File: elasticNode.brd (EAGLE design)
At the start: 58.2 x 52.5 mm, 117 parts, among them J1 FEMALE_HEADER_2X1, J2 JUMPER, J3 ISP_CONN_6PIN, J4 FEMALE_HEADER_3X2, J5 FEMALE_HEADER_10X2, J6 USB_CONNMICRO_SMT, M1 SISS23DN, M2 SISS23DN, M3 SISS23DN, U1 AT90USB128, U10 LTC3419DFN, U11 PAC1720, U12 MT41J128M8, U14 LTC3419DFN, U2 ATMEGA64AQFN, U3 MRF24J40MA, U4 SPARTAN7-LX15, U6 SST26VF032BWDFN, U7 PAC1720, U8 PAC1720, U9 PAC1720, X1 8MHz, X2 50MHz, X3 32MHz, X4 100MHz

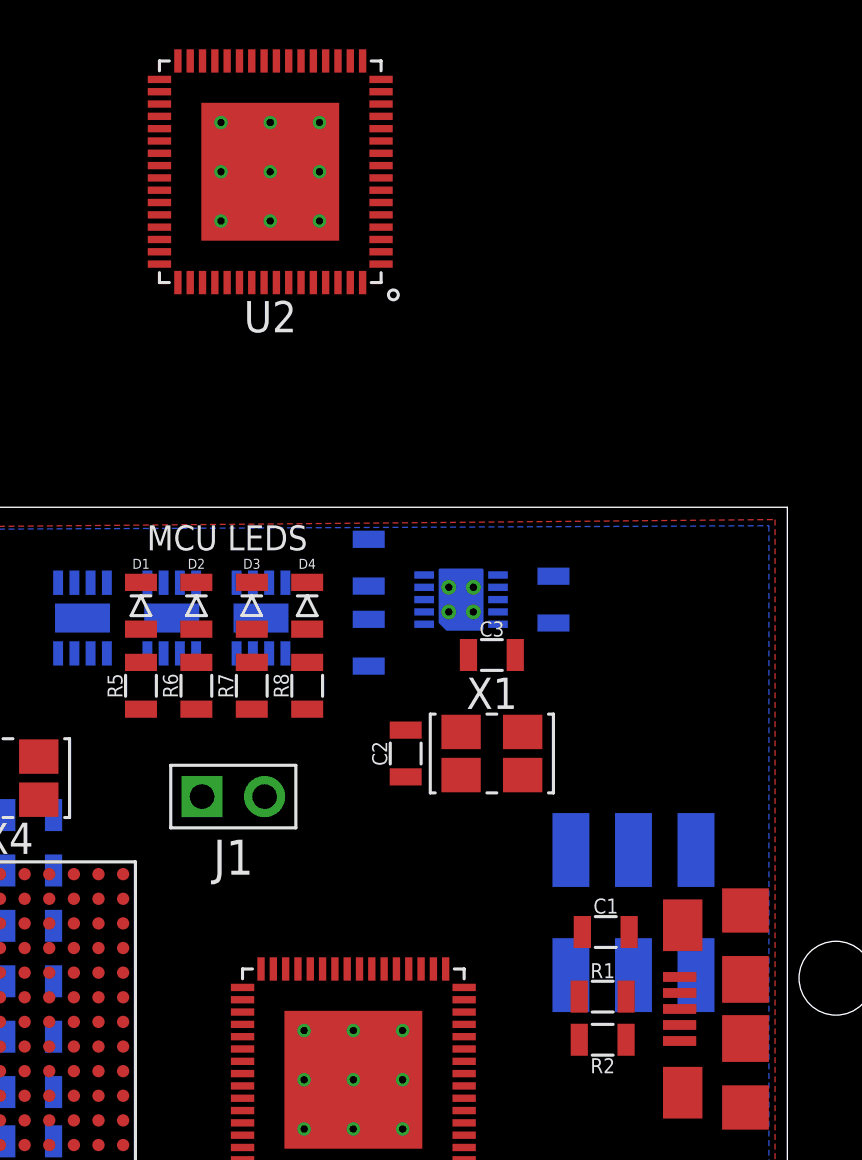
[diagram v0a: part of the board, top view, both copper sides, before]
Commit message: Remove old MCU
 working on the mother board interface.
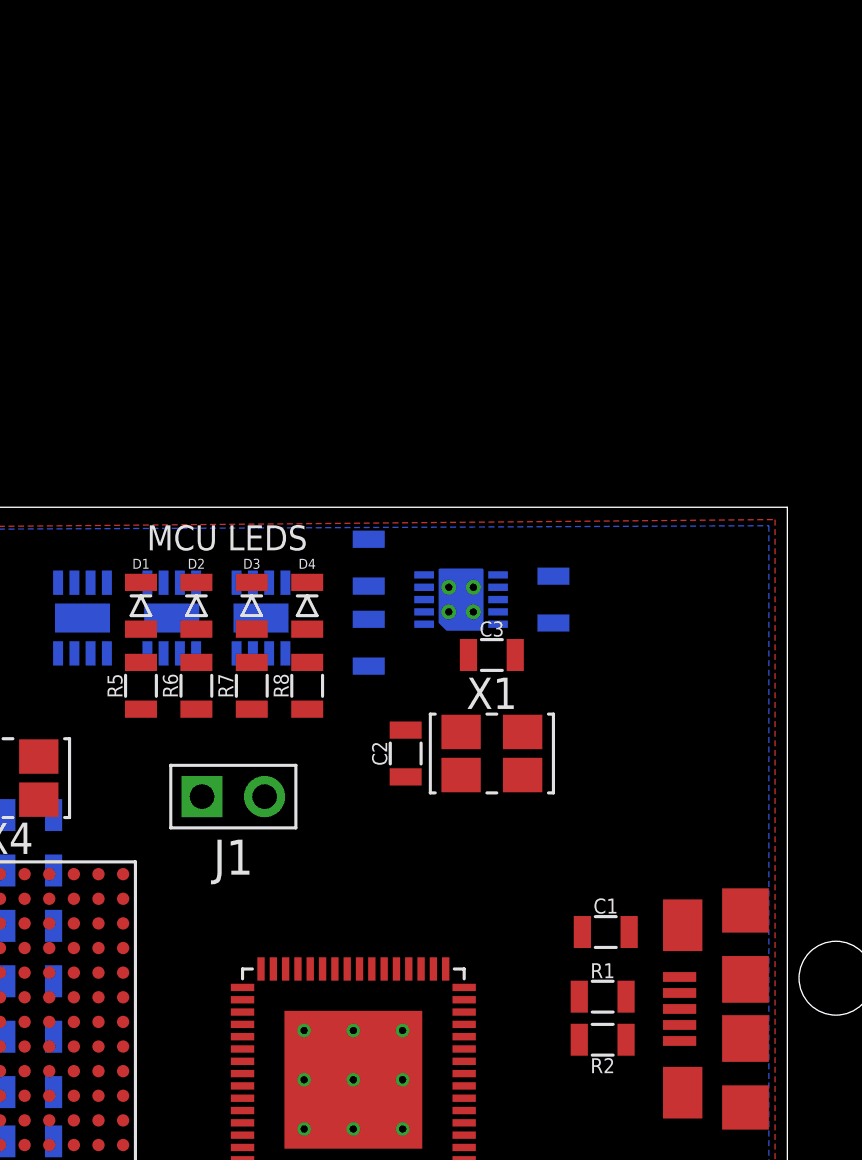
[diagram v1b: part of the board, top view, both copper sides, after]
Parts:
- removed J4: FEMALE_HEADER_3X2, connectors:3X2_HEADER_SMT
- removed U2: ATMEGA64AQFN, ic:QFN64
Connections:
- removed net MCU_GPIO_0: J4.1, U1.19
- removed net MCU_GPIO_1: J4.2, U1.18
- removed net MCU_GPIO_2: J4.3, U1.17
- removed net MCU_GPIO_3: J4.4, U1.16
- removed net MCU_GPIO_4: J4.5, U1.15
- removed net MCU_GPIO_5: J4.6, U1.14
- removed net N$9: U1.10
- new net FPGA_RESES: U1.59
- net ENABLE_LEDS: now also U1.17; no longer U2.9
- net FPGA_DONE: now also U1.16; no longer U2.8
- net FPGA_POWER: now also U1.10; no longer U2.5
- net FPGA_RESET: no longer U2.59
- net FPGA_SUSPEND: now also U1.19; no longer U2.7
- net INIT_B: now also U1.58; no longer U2.58
- net MCU_LED0: now also U1.32; no longer U2.32
- net MCU_LED1: now also U1.31; no longer U2.31
- net MCU_LED2: now also U1.30; no longer U2.30
- net MCU_LED3: now also U1.29; no longer U2.29
- net SPI_CS: now also U1.14; no longer U2.14
- net WIRELESS_CS: now also U1.60; no longer U2.60
- net WIRELESS_INT: now also U1.61; no longer U2.61
- net WIRELESS_RESET: now also U1.15; no longer U2.15
- net WIRELESS_WAKE: now also U1.18; no longer U2.4
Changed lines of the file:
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@@
 <?xml version="1.0" encoding="utf-8"?>
 <!DOCTYPE eagle SYSTEM "eagle.dtd">
-<eagle version="9.2.2">
+<eagle version="9.3.1">
 <drawing>
 <settings>
@@
 <attribute name="NAME" x="27.5" y="23.75" size="0.6096" layer="22" font="vector" rot="MR180" align="bottom-center"/>
 </element>
-<element name="U2" library="ic" package="QFN64" value="ATMEGA64AQFN" x="37.25" y="66.125" smashed="yes" rot="R180">
-<attribute name="NAME" x="37.25" y="60.875" size="1.27" layer="25" font="vector" rot="R180" align="bottom-center"/>
-</element>
 <element name="U6" library="ic" package="WDFN8" value="SST26VF032BWDFN" x="35" y="19.25" smashed="yes" rot="R180">
 <attribute name="NAME" x="35" y="16.25" size="0.8128" layer="25" rot="R180" align="bottom-center"/>
@@
 <attribute name="NAME" x="35.75" y="39" size="1.4224" layer="21" rot="R180" align="bottom-center"/>
 </element>
-<element name="J4" library="connectors" package="3X2_HEADER_SMT" value="FEMALE_HEADER_3X2" x="52" y="36" smashed="yes" rot="MR180"/>
 <element name="U12" library="ic" package="FBGA78DA" value="MT41J128M8" x="8.4" y="28.65" smashed="yes" rot="R270"/>
 <element name="TP6" library="connectors" package="THT" value="TEST_POINTTHT" x="-14.5" y="-34.75" smashed="yes">
@@
 </signal>
 <signal name="INIT_B">
-<contactref element="U2" pad="58"/>
 <contactref element="U4" pad="P8"/>
 <contactref element="R10" pad="1"/>
-<wire x1="25.7" y1="50.125" x2="38" y2="61.625" width="0" layer="19" extent="1-1"/>
+<contactref element="U1" pad="58"/>
 <wire x1="25.275" y1="22.6" x2="25.7" y2="50.125" width="0" layer="19" extent="1-1"/>
+<wire x1="41.375" y1="24.75" x2="25.275" y2="22.6" width="0" layer="19" extent="1-1"/>
 </signal>
 <signal name="AD2/SELECTMAP_D5/MCU_RX1">
@@
 <contactref element="U3" pad="8"/>
 <contactref element="R3" pad="2"/>
-<contactref element="U2" pad="60"/>
-<wire x1="47.5" y1="24.25" x2="39" y2="61.625" width="0" layer="19" extent="1-16"/>
+<contactref element="U1" pad="60"/>
 <wire x1="46.69" y1="19.89" x2="47.5" y2="24.25" width="0" layer="19" extent="16-16"/>
+<wire x1="42.375" y1="24.75" x2="47.5" y2="24.25" width="0" layer="19" extent="1-16"/>
 </signal>
 <signal name="WIRELESS_VCC" class="1" airwireshidden="yes">
@@
 <signal name="WIRELESS_RESET">
 <contactref element="U3" pad="2"/>
-<contactref element="U2" pad="15"/>
-<wire x1="54.31" y1="2.11" x2="41.75" y2="69.375" width="0" layer="19" extent="1-16"/>
+<contactref element="U1" pad="15"/>
+<wire x1="54.31" y1="2.11" x2="45.125" y2="32.5" width="0" layer="19" extent="1-16"/>
 </signal>
 <signal name="WIRELESS_WAKE">
 <contactref element="U3" pad="3"/>
-<contactref element="U2" pad="4"/>
-<wire x1="51.77" y1="2.11" x2="41.75" y2="63.875" width="0" layer="19" extent="1-16"/>
+<contactref element="U1" pad="18"/>
+<wire x1="51.77" y1="2.11" x2="43.875" y2="33.75" width="0" layer="19" extent="1-16"/>
 </signal>
 <signal name="WIRELESS_INT">
 <contactref element="U3" pad="4"/>
-<contactref element="U2" pad="61"/>
-<wire x1="49.23" y1="2.11" x2="39.5" y2="61.625" width="0" layer="19" extent="1-16"/>
+<contactref element="U1" pad="61"/>
+<wire x1="49.23" y1="2.11" x2="42.875" y2="24.75" width="0" layer="19" extent="1-16"/>
 </signal>
 <signal name="USBD+">
@@
 <contactref element="S2" pad="2"/>
 <contactref element="R15" pad="1"/>
-<contactref element="U2" pad="59"/>
 <contactref element="U4" pad="L7"/>
-<wire x1="24.275" y1="26.6" x2="38.5" y2="61.625" width="0" layer="19" extent="1-1"/>
-<wire x1="41.59" y1="13.75" x2="24.275" y2="26.6" width="0" layer="19" extent="1-1"/>
-<wire x1="44.95" y1="18" x2="41.59" y2="13.75" width="0" layer="19" extent="1-1"/>
+<wire x1="41.59" y1="13.75" x2="44.95" y2="18" width="0" layer="19" extent="1-1"/>
+<wire x1="24.275" y1="26.6" x2="41.59" y2="13.75" width="0" layer="19" extent="1-1"/>
 </signal>
 <signal name="FPGA_SUSPEND">
-<contactref element="U2" pad="7"/>
+<contactref element="U1" pad="19"/>
 </signal>
 <signal name="N$1">
@@
 <wire x1="13.23" y1="1.175" x2="28.275" y2="25.6" width="0" layer="19" extent="1-1"/>
 </signal>
-<signal name="MCU_GPIO_0">
-<contactref element="U1" pad="19"/>
-<contactref element="J4" pad="1"/>
-<wire x1="43.375" y1="33.75" x2="49.46" y2="38.58" width="0" layer="19" extent="1-16"/>
-</signal>
-<signal name="MCU_GPIO_1">
-<contactref element="U1" pad="18"/>
-<contactref element="J4" pad="2"/>
-<wire x1="43.875" y1="33.75" x2="52" y2="38.58" width="0" layer="19" extent="1-16"/>
-</signal>
-<signal name="MCU_GPIO_2">
-<contactref element="U1" pad="17"/>
-<contactref element="J4" pad="3"/>
-<wire x1="44.375" y1="33.75" x2="54.54" y2="38.58" width="0" layer="19" extent="1-16"/>
-</signal>
-<signal name="MCU_GPIO_3">
-<contactref element="U1" pad="16"/>
-<contactref element="J4" pad="4"/>
-<wire x1="45.125" y1="33" x2="54.54" y2="33.5" width="0" layer="19" extent="1-16"/>
-</signal>
 <signal name="OSC_32">
 <contactref element="X3" pad="3"/>
@@
 <signal name="MCU_LED0">
 <contactref element="R5" pad="1"/>
-<contactref element="U2" pad="32"/>
-<wire x1="32" y1="44.3" x2="33.5" y2="70.625" width="0" layer="19" extent="1-1"/>
+<contactref element="U1" pad="32"/>
+<wire x1="36.875" y1="33.75" x2="32" y2="44.3" width="0" layer="19" extent="1-1"/>
 </signal>
 <signal name="MCU_LED1">
 <contactref element="R6" pad="1"/>
-<contactref element="U2" pad="31"/>
-<wire x1="34.25" y1="44.3" x2="34" y2="70.625" width="0" layer="19" extent="1-1"/>
+<contactref element="U1" pad="31"/>
+<wire x1="37.375" y1="33.75" x2="34.25" y2="44.3" width="0" layer="19" extent="1-1"/>
 </signal>
 <signal name="MCU_LED2">
 <contactref element="R7" pad="1"/>
-<contactref element="U2" pad="30"/>
-<wire x1="36.5" y1="44.3" x2="34.5" y2="70.625" width="0" layer="19" extent="1-1"/>
+<contactref element="U1" pad="30"/>
+<wire x1="37.875" y1="33.75" x2="36.5" y2="44.3" width="0" layer="19" extent="1-1"/>
 </signal>
 <signal name="MCU_LED3">
 <contactref element="R8" pad="1"/>
-<contactref element="U2" pad="29"/>
-<wire x1="38.75" y1="44.3" x2="35" y2="70.625" width="0" layer="19" extent="1-1"/>
+<contactref element="U1" pad="29"/>
+<wire x1="38.375" y1="33.75" x2="38.75" y2="44.3" width="0" layer="19" extent="1-1"/>
 </signal>
 <signal name="N$32">
@@
 </signal>
 <signal name="ENABLE_LEDS">
-<contactref element="U2" pad="9"/>
+<contactref element="U1" pad="17"/>
 </signal>
 <signal name="MONITORING">
@@
 <contactref element="M1" pad="4"/>
 <contactref element="M2" pad="4"/>
-<contactref element="U2" pad="5"/>
 <contactref element="M3" pad="4"/>
-<wire x1="35.885" y1="46.565" x2="41.75" y2="64.375" width="0" layer="19" extent="1-16"/>
+<contactref element="U1" pad="10"/>
 <wire x1="32.26" y1="46.565" x2="35.885" y2="46.565" width="0" layer="19" extent="16-16"/>
 <wire x1="28.635" y1="46.565" x2="32.26" y2="46.565" width="0" layer="19" extent="16-16"/>
+<wire x1="45.125" y1="30" x2="35.885" y2="46.565" width="0" layer="19" extent="1-16"/>
 </signal>
 <signal name="FPGA_VCCAUX_MON">
@@
 </signal>
 <signal name="FPGA_DONE">
-<contactref element="U2" pad="8"/>
 <contactref element="U4" pad="P9"/>
-<wire x1="26.275" y1="22.6" x2="41.75" y2="65.875" width="0" layer="19" extent="1-1"/>
+<contactref element="U1" pad="16"/>
+<wire x1="26.275" y1="22.6" x2="45.125" y2="33" width="0" layer="19" extent="1-1"/>
 </signal>
 <signal name="N$4">
@@
 <wire x1="45.125" y1="29.5" x2="53.875" y2="32.775" width="0" layer="19" extent="1-1"/>
 </signal>
-<signal name="N$9">
-<contactref element="U1" pad="10"/>
-</signal>
 <signal name="N$3">
 <contactref element="R2" pad="2"/>
@@
 <contactref element="R19" pad="2"/>
 <contactref element="U4" pad="L14"/>
-<contactref element="U2" pad="14"/>
-<wire x1="28.275" y1="35.6" x2="41.75" y2="68.875" width="0" layer="19" extent="1-1"/>
-<wire x1="31.275" y1="26.6" x2="28.275" y2="35.6" width="0" layer="19" extent="1-1"/>
-<wire x1="38" y1="17.345" x2="28.275" y2="35.6" width="0" layer="19" extent="1-1"/>
-<wire x1="39.8" y1="18.75" x2="38" y2="17.345" width="0" layer="19" extent="1-1"/>
+<contactref element="U1" pad="14"/>
+<wire x1="39.8" y1="18.75" x2="45.125" y2="32" width="0" layer="19" extent="1-1"/>
+<wire x1="38" y1="17.345" x2="39.8" y2="18.75" width="0" layer="19" extent="1-1"/>
+<wire x1="31.275" y1="26.6" x2="38" y2="17.345" width="0" layer="19" extent="1-1"/>
+<wire x1="28.275" y1="35.6" x2="31.275" y2="26.6" width="0" layer="19" extent="1-1"/>
 </signal>
 <signal name="SPI_SCK/CCLK">
@@
 <wire x1="-10.3" y1="-52" x2="-10.3" y2="-49.25" width="0" layer="19" extent="1-1"/>
 </signal>
-<signal name="MCU_GPIO_4">
-<contactref element="U1" pad="15"/>
-<contactref element="J4" pad="5"/>
-<wire x1="45.125" y1="32.5" x2="52" y2="33.5" width="0" layer="19" extent="1-16"/>
-</signal>
-<signal name="MCU_GPIO_5">
-<contactref element="U1" pad="14"/>
-<contactref element="J4" pad="6"/>
-<wire x1="45.125" y1="32" x2="49.46" y2="33.5" width="0" layer="19" extent="1-16"/>
-</signal>
 <signal name="DDR_DQS_N">
 <contactref element="U12" pad="D3"/>
@@
 <contactref element="U4" pad="J3"/>
 </signal>
+<signal name="FPGA_RESES">
+<contactref element="U1" pad="59"/>
+</signal>
 </signals>

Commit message: backup before review
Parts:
- removed 1000: 6k8, passive:0805
- removed 2.2K: 1k5, passive:0805
- removed C12, C9: 10u, passive:0805
- removed C15: 4.7u, passive:0805
- removed C6: 100u, passive:1210
- removed U12: MT41J128M8, ic:FBGA78DA
- added C20, C31, C32, C33, C37, C38, C39: 0.47u, passive:0805
- added C24, C34: 100u, passive:1210
- added C25, C29, C30, C35, C36, C40: 4.7u, passive:0805
- added OUT1, OUT2: FEMALE_HEADER_5X2, connectors:5X2_HEADER_SMT_1.27
- added R46: 10k, passive:0805
- added R47: 20k, passive:0805
- added R48, R49: 1.5k, passive:0805
- added U2: IS66WV51216EALL, ic:TSOP44
- C1: value (none) -> 10u
- C13: value 10u -> 0.47u
- C16: value 2.2u -> 0.47u
- C7: value 47u -> 4.7u
- R34: value 1k5 -> 10k
- R39: value 1k5 -> 6k8
- R41, R42: value 10k -> 1.5k
- R44: value 240%1 -> 1.5k
- R45: value 80.6 -> 1.5k
- moved R15 160.0 mm to (-28.0, -124.9), turned to 0 degrees
- moved S2 148.2 mm to (-23.6, -121.5)
- moved R29 147.4 mm to (-28.0, -132.7), flipped to the top, turned to 0 degrees
- moved R30 147.3 mm to (-28.0, -135.3), flipped to the top, turned to 0 degrees
- moved R44 66.4 mm to (-28.0, -137.9)
- moved R45 66.3 mm to (-28.0, -140.5)
- moved R41 61.7 mm to (-28.0, -127.5)
- moved R42 61.5 mm to (-28.0, -130.1)
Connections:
- removed net DDR_A0: U12.K3, U4.B3
- removed net DDR_A1: U12.L7, U4.N1
- removed net DDR_A10: U12.H7, U4.M2
- removed net DDR_A11: U12.M7, U4.P2
- removed net DDR_A12: U12.K7, U4.M4
- removed net DDR_A13: U12.N3, U4.A5
- removed net DDR_A2: U12.L3, U4.B6
- removed net DDR_A3: U12.K2, U4.B2, U4.F4
- removed net DDR_A4: U12.L8, U4.M5
- removed net DDR_A5: U12.L2, U4.B5
- removed net DDR_A6: U12.M8, U4.N4
- removed net DDR_A7: U12.M2, U4.A2
- removed net DDR_A8: U12.N8, U4.P5
- removed net DDR_A9: U12.M3, U4.A3
- removed net DDR_BA0: U12.J2, U4.C5
- removed net DDR_BA1: U12.K8, U4.M3
- removed net DDR_BA2: U12.J3, U4.B1
- removed net DDR_CAS: U12.G3, U4.C1
- removed net DDR_CKE: U12.G9, U4.M1
- removed net DDR_CLK_N: R45.1, U12.G7, U4.P3
- removed net DDR_CLK_P: R45.2, U12.F7, U4.P4
- removed net DDR_CS: U12.H2, U4.C3
- removed net DDR_DQ0: U12.B3, U4.E2
- removed net DDR_DQ1: U12.C7, U4.L2
- removed net DDR_DQ2: U12.C2, U4.E4
- removed net DDR_DQ3: U12.C8, U4.L1
- removed net DDR_DQ4: U12.E3, U4.D2
- removed net DDR_DQ5: U12.E8, U4.L3
- removed net DDR_DQ6: U12.D2, U4.D1
- removed net DDR_DQ7: U12.E7, U4.L5
- removed net DDR_DQS_N: U12.D3, U4.F1
- removed net DDR_DQS_P: U12.C3, U4.G1
- removed net DDR_ODT: U12.G1, U4.D4
- removed net DDR_RAS: U12.F3, U4.D3
- removed net DDR_RESET: U12.N2, U4.A4
- removed net DDR_WE: U12.H3, U4.C4
- removed net N$18: U4.B10
- removed net N$37: U4.H14
- removed net N$38: U4.H13
- removed net N$43: U4.F3
- removed net N$44: U4.F2
- removed net N$52: U4.H4
- removed net N$58: U4.C12
- removed net N$59: U4.H3
- removed net N$60: U4.H2
- removed net N$61: U4.H1
- removed net N$62: U4.J2
- removed net N$63: U4.J1
- removed net N$64: U4.K4
- removed net N$65: U4.K3
- removed net N$66: U4.J4
- removed net N$67: U4.J3
- removed net N$69: R44.1, U12.H8
- removed net VCC_DDR: R23.2, R41.2, R43.2, U11.2, U12.A2, U12.A9, U12.B9, U12.C1, U12.D7, U12.E2, U12.E9, U12.G2, U12.G8, U12.K1, U12.K9, U12.M1, U12.M9, U4.G2, U4.K2, U4.N2, U7.2, X4.1, X4.4
- removed net VREF_DDR: R41.1, R42.2, U12.E1, U12.J8
- new net 1V8: C19.2, L2.2, R23.1, R25.2, R43.1, R47.2, TP2.3, U11.1, U7.1, U9.1
- new net N$21: U4.P4
- new net N$22: U4.P3
- new net N$26: U4.L3
- new net N$31: U4.L2
- new net N$33: U4.M5
- new net N$34: U4.M4
- new net N$35: U4.P5
- new net N$36: U4.N4
- new net N$40: U4.L5
- new net SRAM_A0: U2.5, U4.D3
- new net SRAM_A1: U2.4, U4.C3
- new net SRAM_A10: U2.25, U4.C5
- new net SRAM_A11: U2.24, U4.C4
- new net SRAM_A12: U2.22, U4.E4
- new net SRAM_A13: U2.21, U4.D4
- new net SRAM_A14: U2.20, U4.F3
- new net SRAM_A15: U2.19, U4.F2
- new net SRAM_A16: U2.18, U4.G1
- new net SRAM_A17: U2.23, U4.F1
- new net SRAM_A18: U2.28, U4.E2
- new net SRAM_A2: U2.3, U4.A4
- new net SRAM_A3: U2.2, U4.A3
- new net SRAM_A4: U2.1, U4.B3
- new net SRAM_A5: U2.44, U4.A2
- new net SRAM_A6: U2.43, U4.B5
- new net SRAM_A7: U2.42, U4.A5
- new net SRAM_A8: U2.27, U4.B2
- new net SRAM_A9: U2.26, U4.B1
- new net SRAM_CS: U2.6, U4.B6
- new net SRAM_D0: U2.7, U4.D2
- new net SRAM_D1: U2.8, U4.D1
- new net SRAM_D10: U2.31, U4.K3
- new net SRAM_D11: U2.32, U4.J4
- new net SRAM_D12: U2.35, U4.J3
- new net SRAM_D13: U2.36, U4.M1
- new net SRAM_D14: U2.37, U4.L1
- new net SRAM_D15: U2.38, U4.M3
- new net SRAM_D2: U2.9, U4.C1
- new net SRAM_D3: U2.10, U4.H4
- new net SRAM_D4: U2.13, U4.H3
- new net SRAM_D5: U2.14, U4.H2
- new net SRAM_D6: U2.15, U4.H1
- new net SRAM_D7: U2.16, U4.J2
- new net SRAM_D8: U2.29, U4.J1
- new net SRAM_D9: U2.30, U4.K4
- new net SRAM_LB: U2.39, U4.N1
- new net SRAM_OE: U2.41, U4.M2
- new net SRAM_UB: U2.40, U4.P2
- new net SRAM_VCC: R23.2, R43.2, U11.2, U4.G2, U4.K2, U4.N2, U7.2, X4.1, X4.4
- new net SRAM_VDD: C24.1, C25.1, C29.1, C30.1, C31.1, C32.1, C33.1, U2.11, U2.33
- new net SRAM_WE: U2.17, U4.F4
- net 1V: now also R46.2; no longer 1000.1
- net 1V2: no longer R25.2, U9.1
- net 1V5: no longer 2.2K.2, C19.2, L2.2, R23.1, R43.1, U11.1, U7.1
- net 3V3: now also OUT2.10, R30.2, R41.2, R42.2, R44.2, R45.2, R48.2, R49.2; no longer R30.1, TP2.3
- net 5V: now also OUT2.9, R36.2, U11.3; no longer R36.1, U11.4
- net A10: now also OUT1.5
- net A11: now also OUT1.6
- net A12: now also OUT1.7
- net A13: now also OUT1.8
- net A14: now also OUT1.10
- net A8: now also OUT1.3
- net A9: now also OUT1.4
- net AD0/SELECTMAP_D7: now also OUT2.1
- net AD1/SELECTMAP_D6: now also OUT2.2
- net AD2/SELECTMAP_D5/MCU_RX1: now also OUT2.3
- net AD3/SELECTMAP_D4/MCU_TX1: now also OUT2.4
- net AD4/SELECTMAP_D3/FPGA_HOLD: now also OUT2.5
- net AD5/SELECTMAP_D2/FPGA_WP: now also OUT2.6
- net ALE/HWB: now also OUT1.9
- net FPGA_GPIO_18: now also U4.H14
- net FPGA_GPIO_19: now also U4.H13
- net FPGA_LED0: now also U4.E11
- net FPGA_LED1: now also U4.B10
- net FPGA_LED2: now also U4.A10
- net FPGA_LED3: now also U4.C12
- net FPGA_VCCAUX: now also C20.1
- net FPGA_VCCIO: now also C34.1, C35.1, C36.1, C37.1, C38.1, C39.1, C40.1; no longer C12.1, C15.1, C6.1, C9.1, R20.1, U7.4
- net FPGA_VCCIO_MON: now also R20.1, U7.4
- net GND: now also C20.2, C24.2, C25.2, C29.2, C30.2, C31.2, C32.2, C33.2, C34.2, C35.2, C36.2, C37.2, C38.2, C39.2, C40.2, OUT2.7, OUT2.8, U2.12, U2.34; no longer C12.2, C15.2, C6.2, C9.2, R42.1, R44.2, U12.A1, U12.A8, U12.B1, U12.B2, U12.B7, U12.B8, U12.C9, U12.D1, U12.D8, U12.D9, U12.F2, U12.F8, U12.J1, U12.J9, U12.L1, U12.L9, U12.N1, U12.N9
- net N$53: now also R46.1; no longer 1000.2
- net N$7: now also R47.1; no longer 2.2K.1
- net SCL: now also OUT1.1, R41.1, R44.1, R48.1
- net SDA: now also OUT1.2, R30.1, R42.1, R45.1, R49.1; no longer R30.2
- net USB_VCC_RAW: now also R36.1, U11.4; no longer R36.2, U11.3
